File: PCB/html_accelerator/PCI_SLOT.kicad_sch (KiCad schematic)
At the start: 3 parts, among them J2 Bus_PCI_Express_x8, J3 PCIexpress_bracket, U1 MCS9990

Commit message: Schematic edits
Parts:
- removed unit 5 of U1
- removed unit 4 of U1
- removed unit 2 of U1
- removed unit 1 of U1
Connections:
- net GND: now reaches J3.1 (PTH1)
- net GND: now also J2.A12 (GND), J2.A15 (GND), J2.A18 (GND), J2.A20 (GND), J2.A23 (GND), J2.A24 (GND), J2.A27 (GND), J2.A28 (GND), J2.A31 (GND), J2.A34 (GND), J2.A37 (GND), J2.A38 (GND), J2.A4 (GND), J2.A41 (GND), J2.A42 (GND), J2.A45 (GND), J2.A46 (GND), J2.A49 (GND), J2.B13 (GND), J2.B16 (GND), J2.B18 (GND), J2.B21 (GND), J2.B22 (GND), J2.B25 (GND), J2.B26 (GND), J2.B29 (GND), J2.B32 (GND), J2.B35 (GND), J2.B36 (GND), J2.B39 (GND), J2.B4 (GND), J2.B40 (GND), J2.B43 (GND), J2.B44 (GND), J2.B47 (GND), J2.B49 (GND), J2.B7 (GND), J3.2 (PTH2)
- net +3V3: now reaches J2.A10 (+3.3V), J2.A9 (+3.3V), J2.B8 (+3.3V)
- net +3V3: now also J2.B10 (3.3Vaux)
- net +12V: now reaches J2.A2 (+12V), J2.A3 (+12V), J2.B1 (+12V), J2.B2 (+12V), J2.B3 (+12V)
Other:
- moved on the sheet: J2, J3, U1C

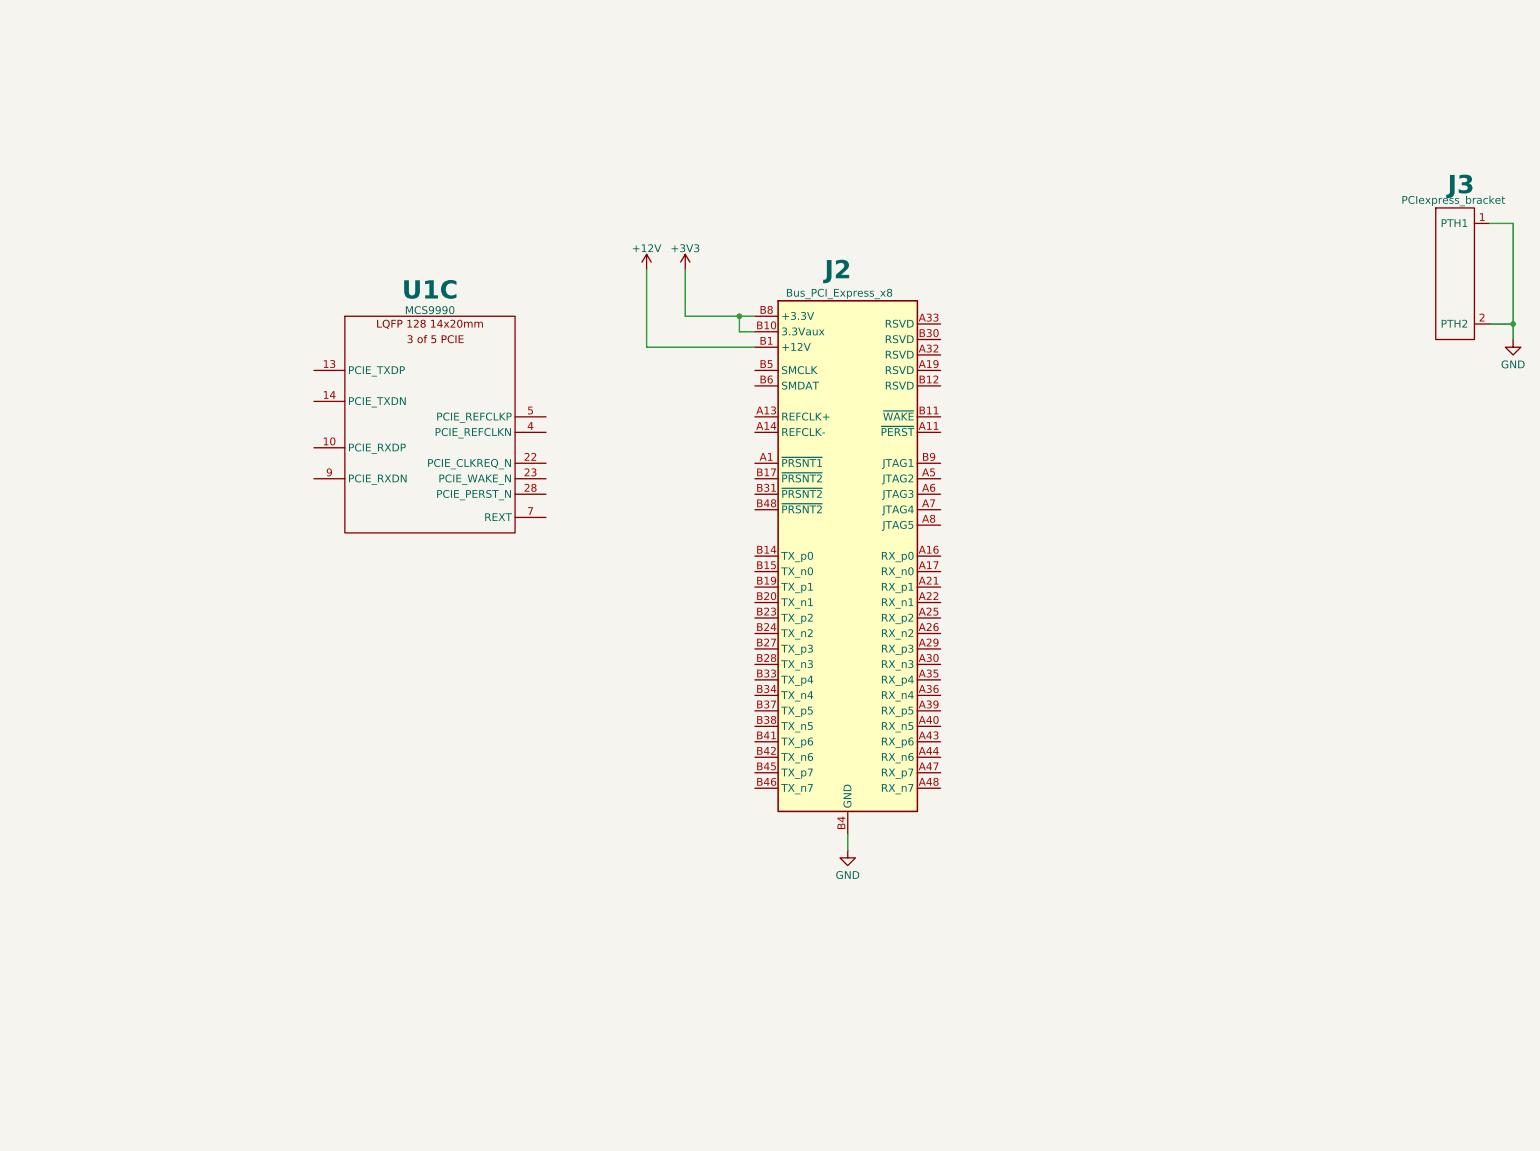
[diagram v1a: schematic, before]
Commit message: PCIE connections wired
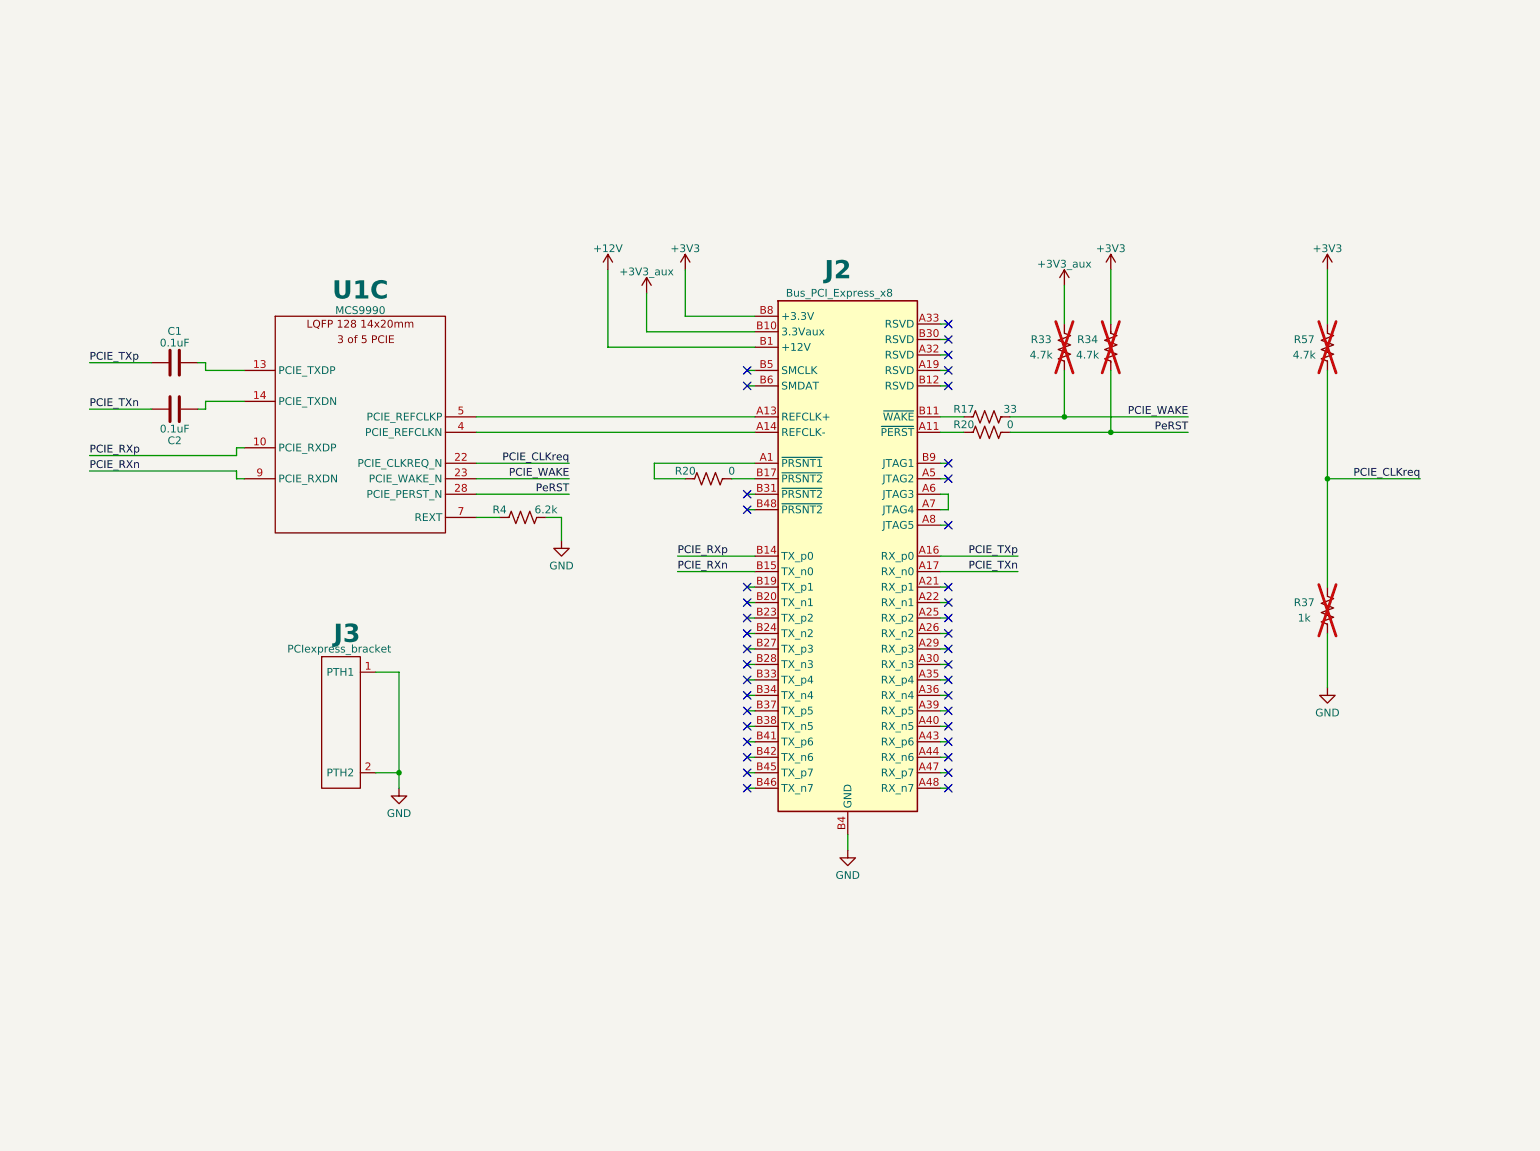
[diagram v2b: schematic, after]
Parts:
- added C1, C2: 0.1uF, symbol Device:C
- added R17: 33, symbol Device:R_US
- added R20 (x2): 0, symbol Device:R_US
- added R33, R34, R57: 4.7k, symbol Device:R_US
- added R37: 1k, symbol Device:R_US
- added R4: 6.2k, symbol Device:R_US
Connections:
- net +3V3: now also R33.2, R34.2, R57.2
- net GND: now also R37.1, R4.2
- net PCIE_RXp: now reaches U1.10 (PCIE_RXDP)
- net PCIE_RXp: now also J2.B14 (TX_p0)
- net at U1.13 (PCIE_TXDP): now also C1.2
- net at U1.14 (PCIE_TXDN): now also C2.2
- net PCIE_CLKreq: now reaches U1.22 (PCIE_CLKREQ_N)
- net PCIE_CLKreq: now also R37.2, R57.1
- net PCIE_WAKE: now reaches U1.23 (PCIE_WAKE_N)
- net PCIE_WAKE: now also R17.2, R33.1
- net PeRST: now reaches U1.28 (PCIE_PERST_N)
- net PeRST: now also R20.2, R34.1
- net at U1.4 (PCIE_REFCLKN): now also J2.A14 (REFCLK-)
- net at U1.5 (PCIE_REFCLKP): now also J2.A13 (REFCLK+)
- net at U1.7 (REXT): now also R4.1
- net PCIE_RXn: now reaches U1.9 (PCIE_RXDN)
- net PCIE_RXn: now also J2.B15 (TX_n0)
- net at J2.A1 (~{PRSNT1}): now also R20.1
- net at J2.A11 (~{PERST}): now also R20.1
- net PCIE_TXp: now reaches J2.A16 (RX_p0)
- net PCIE_TXp: now also C1.1
- net PCIE_TXn: now reaches J2.A17 (RX_n0)
- net PCIE_TXn: now also C2.1
- net at J2.A6 (JTAG3): now also J2.A7 (JTAG4)
- net at J2.B11 (~{WAKE}): now also R17.1
- net at J2.B17 (~{PRSNT2}): now also R20.2
- no-connect marks 0 -> 40
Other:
- moved on the sheet: J3, U1C

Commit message: schematic updates
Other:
- title: (none) -> PCIE Slot, Bracket
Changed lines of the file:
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@@
 (kicad_sch (version 20230121) (generator eeschema)
   (paper "A4")
+  (title_block
+    (title "PCIE Slot, Bracket")
+    (date "2024-09-15")
+    (rev "1")
+  )
   (junction (at 231.14 90.17) (diameter 0) (color 0 0 0 0)
   )
